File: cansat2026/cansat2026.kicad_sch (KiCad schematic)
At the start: 29 parts, among them J102 MCU_UART_Conn, J103 MCU_CAM_UART_Conn, J104 920MHz_Conn, J105 I2C_Conn, J106 I2C_Conn, J117 CAM_Conn, J121 MCU_Power, J122 MCU_Power, J124 Motor_Power, J126 Micro_SD_Card_Det_Hirose_DM3AT, U101 ESP32-S3-WROOM-1U-N4R8, U102 ESP32-S3-WROOM-1U-N4R8

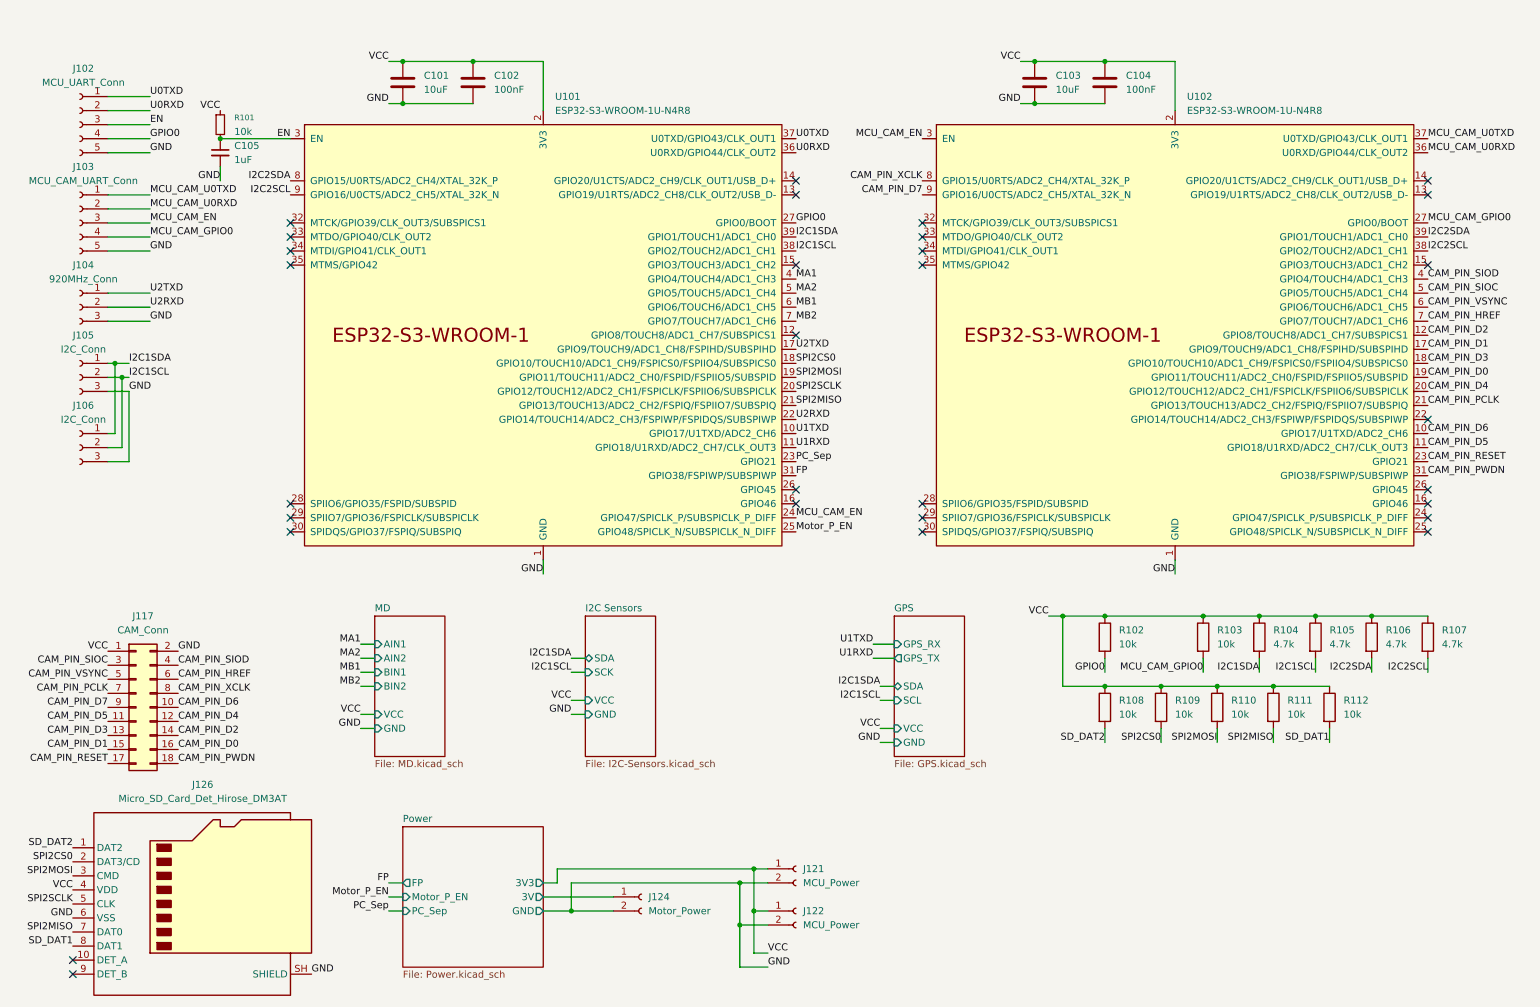
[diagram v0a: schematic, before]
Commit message: Update: MCUシートを作成
MCU部分を分けた
あとでFPGAつけるかもしれないしね
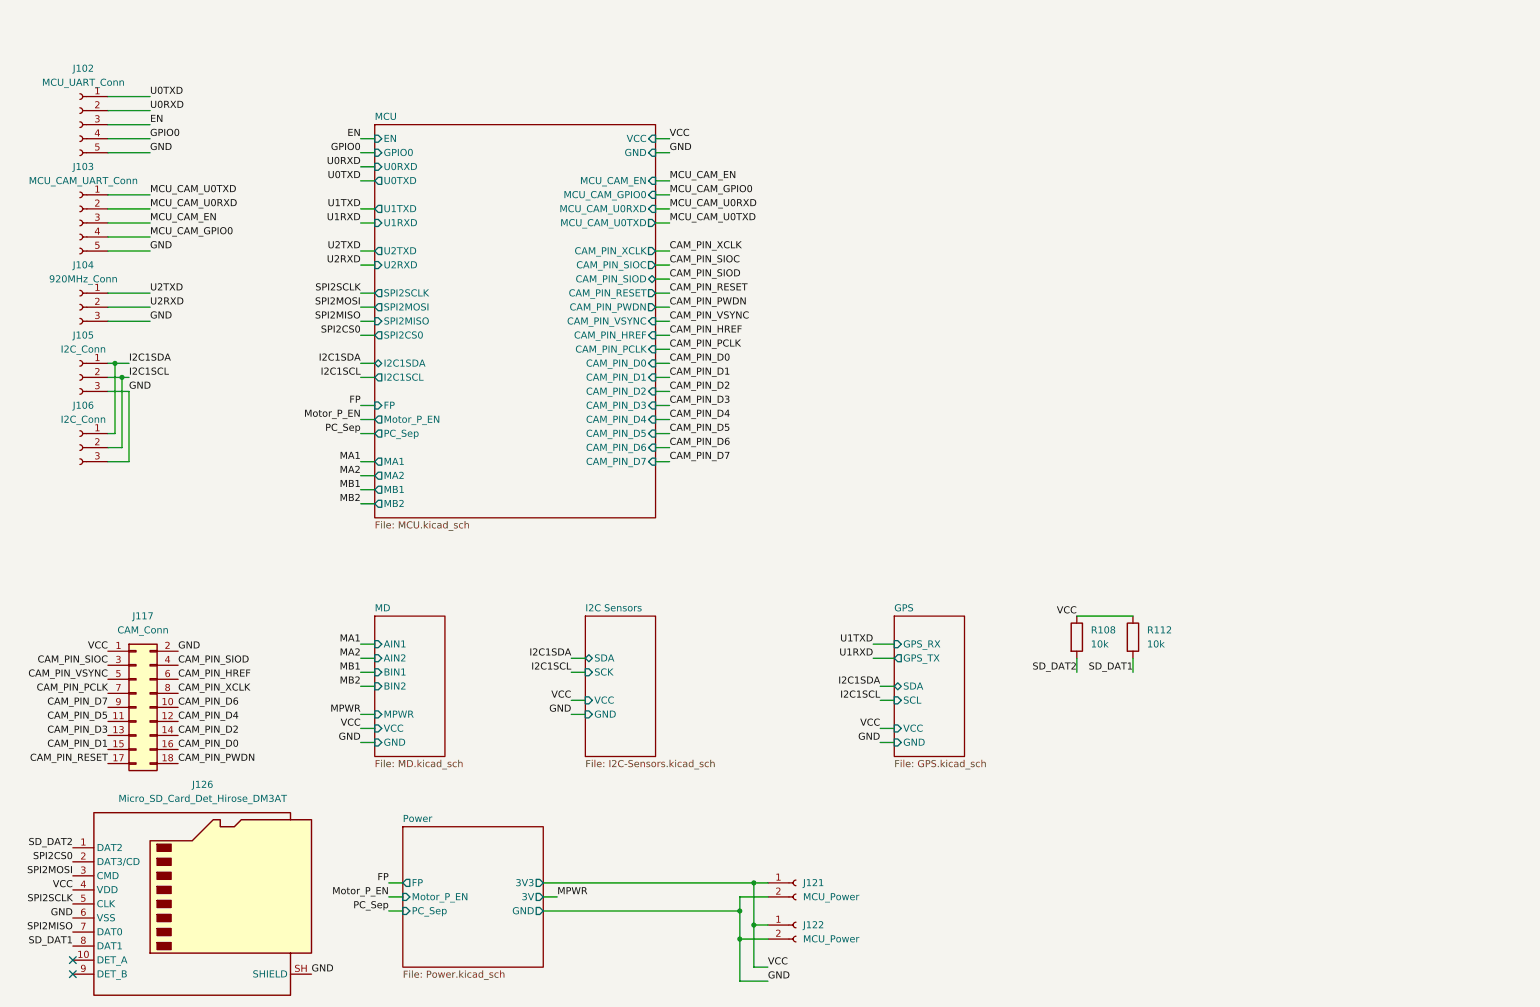
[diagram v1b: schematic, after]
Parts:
- removed C101, C103: 10uF, Capacitor_SMD:C_0402_1005Metric, symbol Device:C
- removed C102, C104: 100nF, Capacitor_SMD:C_0402_1005Metric, symbol Device:C
- removed C105: 1uF, Capacitor_SMD:C_0402_1005Metric, symbol Device:C_Small
- removed J124: Motor_Power, Connector_JST:JST_XH_B2B-XH-A_1x02_P2.50mm_Vertical, symbol Connector:Conn_01x02_Socket
- removed R101: 10k, Resistor_SMD:R_0402_1005Metric, symbol Device:R_Small
- removed R102, R103, R109, R110, R111: 10k, Resistor_SMD:R_0402_1005Metric, symbol Device:R
- removed R104, R105, R106, R107: 4.7k, Resistor_SMD:R_0402_1005Metric, symbol Device:R
- removed U101, U102: ESP32-S3-WROOM-1U-N4R8, PCM_Espressif:ESP32-S3-WROOM-1U, symbol PCM_Espressif:ESP32-S3-WROOM-1
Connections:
- no-connect marks 30 -> 2
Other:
- added sheet MCU (MCU.kicad_sch)
- sheet MD ports: added MPWR; removed none
- moved on the sheet: J121, J122

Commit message: Update: ラベルをワイヤーにした
ラベルが衝突してERCが出たから
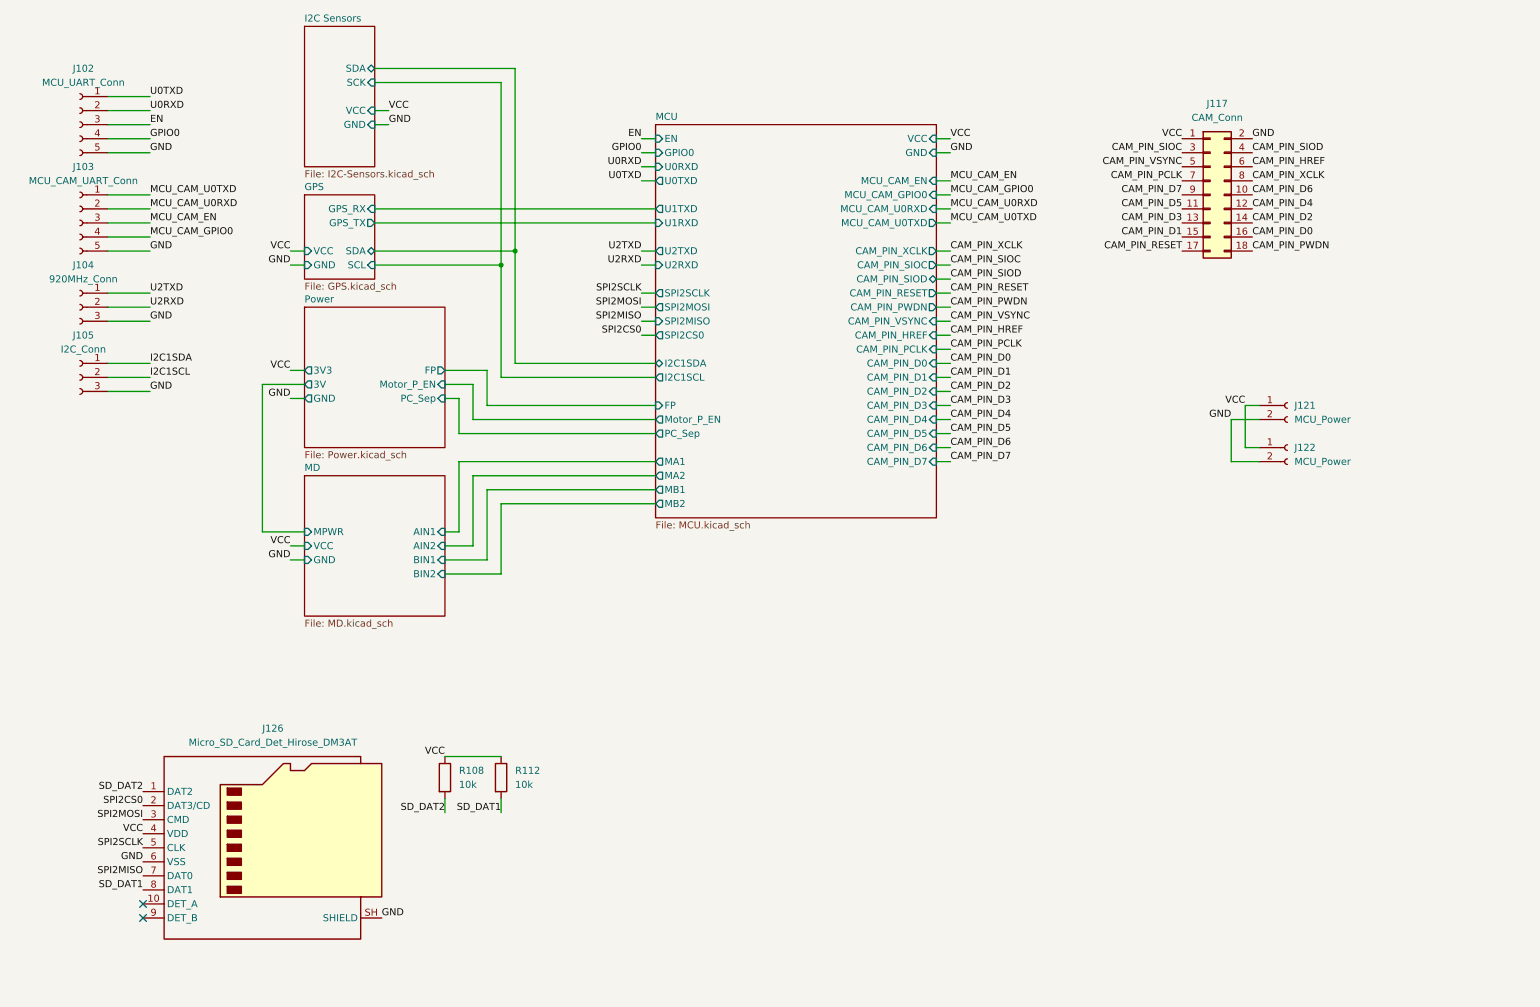
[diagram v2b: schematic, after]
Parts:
- removed J106: I2C_Conn, Connector_JST:JST_XH_B3B-XH-A_1x03_P2.50mm_Vertical, symbol Connector:Conn_01x03_Socket
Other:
- moved on the sheet: J117, J121, J122, J126, R108, R112

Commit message: Update: いろいろした
無線変えた
カメラのコネクタ変えた
i2cセンサ変えた
電源変えた:1.2V,3.8V,3.3V
IOエキスパンダ追加
FPGA追加
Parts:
- removed J104: 920MHz_Conn, Connector_JST:JST_XH_B3B-XH-A_1x03_P2.50mm_Vertical, symbol Connector:Conn_01x03_Socket
- removed J117: CAM_Conn, Connector_PinHeader_2.54mm:PinHeader_2x10_P2.54mm_Vertical, symbol Connector_Generic:Conn_02x09_Odd_Even
- added C101: 100nF, Capacitor_SMD:C_0402_1005Metric, symbol Device:C_Small
- added C102: 100nF, Capacitor_SMD:C_0402_1005Metric, symbol Device:C
- added J102: CAM_Conn, Project:SHOUHAN_XJH2.0_0.43-24P_1x24-1MP_P0.50mm_Horizontal, symbol Connector_Generic_MountingPin:Conn_02x12_Odd_Even_MountingPin
- added J108: Conn_Coaxial, Connector_Coaxial:SMA_Samtec_SMA-J-P-H-ST-EM1_EdgeMount, symbol Connector:Conn_Coaxial
- added U101: E220-900T22S(JP), Project:E220-900T22S(JP), symbol Project:E220-900T22S(JP)
- renumbered J102 to J101, J105 to J104, J121 to J105, J122 to J106, J126 to J107, R108 to R101, R112 to R102
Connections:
- net CAM_PIN_D0: now also J102.23 (Pin_23)
- net CAM_PIN_D1: now also J102.22 (Pin_22)
- net CAM_PIN_D2: now also J102.21 (Pin_21)
- net CAM_PIN_D3: now also J102.20 (Pin_20)
- net CAM_PIN_D4: now also J102.19 (Pin_19)
- net CAM_PIN_D5: now also J102.18 (Pin_18)
- net CAM_PIN_D6: now also J102.17 (Pin_17)
- net CAM_PIN_D7: now also J102.16 (Pin_16)
- net CAM_PIN_HREF: now also J102.12 (Pin_12)
- net CAM_PIN_PCLK: now also J102.14 (Pin_14)
- net CAM_PIN_PWDN: now also J102.5 (Pin_5)
- net CAM_PIN_RESET: now also J102.6 (Pin_6)
- net CAM_PIN_SIOC: now also J102.3 (Pin_3)
- net CAM_PIN_SIOD: now also J102.4 (Pin_4)
- net CAM_PIN_VSYNC: now also J102.11 (Pin_11)
- net CAM_PIN_XCLK: now also J102.8 (Pin_8)
- net GND: now also C101.2, C102.2, J102.13 (Pin_13), J102.15 (Pin_15), J102.24 (Pin_24), J102.7 (Pin_7), J102.9 (Pin_9), J102.MP (MountPin), J108.2 (Ext), U101.1 (GND), U101.11 (GND), U101.19 (GND), U101.2 (GND), U101.20 (GND), U101.22 (GND), U101.3 (GND), U101.4 (GND)
- net U2RXD: now also U101.8 (TXD)
- net U2TXD: now also U101.7 (RXD)
- net VCC: now also J102.1 (Pin_1), J102.2 (Pin_2)
- new net: J108.1 (In), U101.21 (ANT)
- new net: U101.16 (NC), U101.17 (NC), U101.18 (NC)
- new net 3.8V: C101.1, U101.10 (VCC)
- new net COM_AUX: C102.1, U101.9 (AUX)
- new net COM_M0: U101.5 (M0)
- new net COM_M1: U101.6 (M1)
- no-connect marks 2 -> 7
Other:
- sheet MCU ports: added 1.2V, COM_AUX, COM_M0, COM_M1, COM_P_EN; removed none
- sheet Power ports: added 1.2V, 3.8V, COM_P_EN; removed none
- moved on the sheet: J104

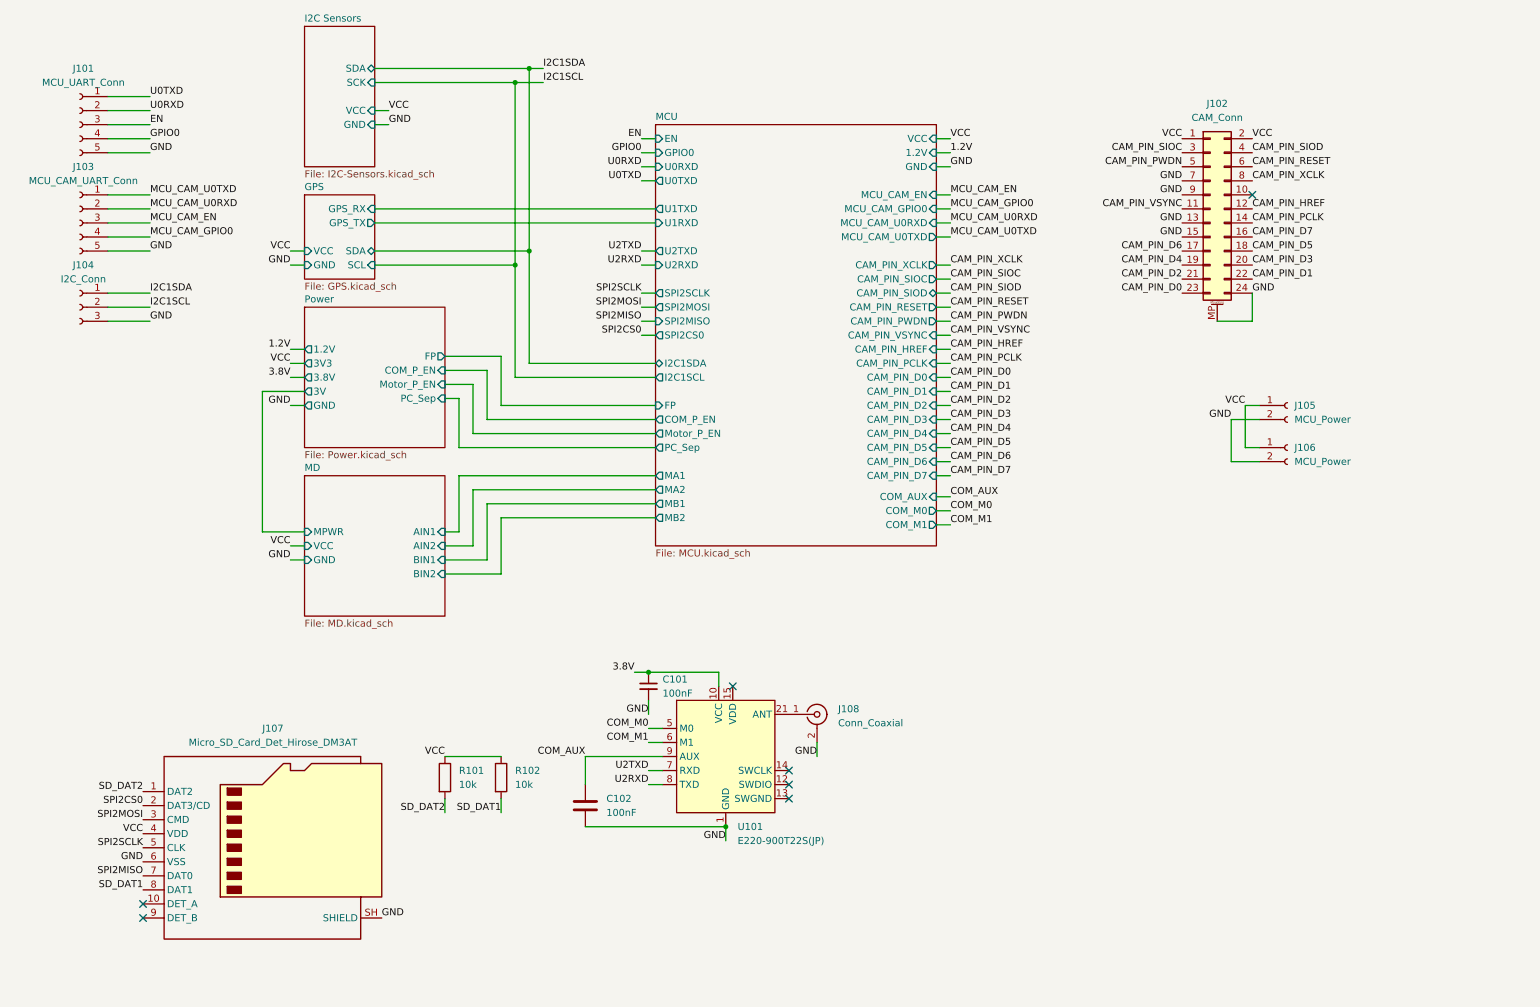
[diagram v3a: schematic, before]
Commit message: Update: MDと電源とか
MD変えた
モーター電源と主電源
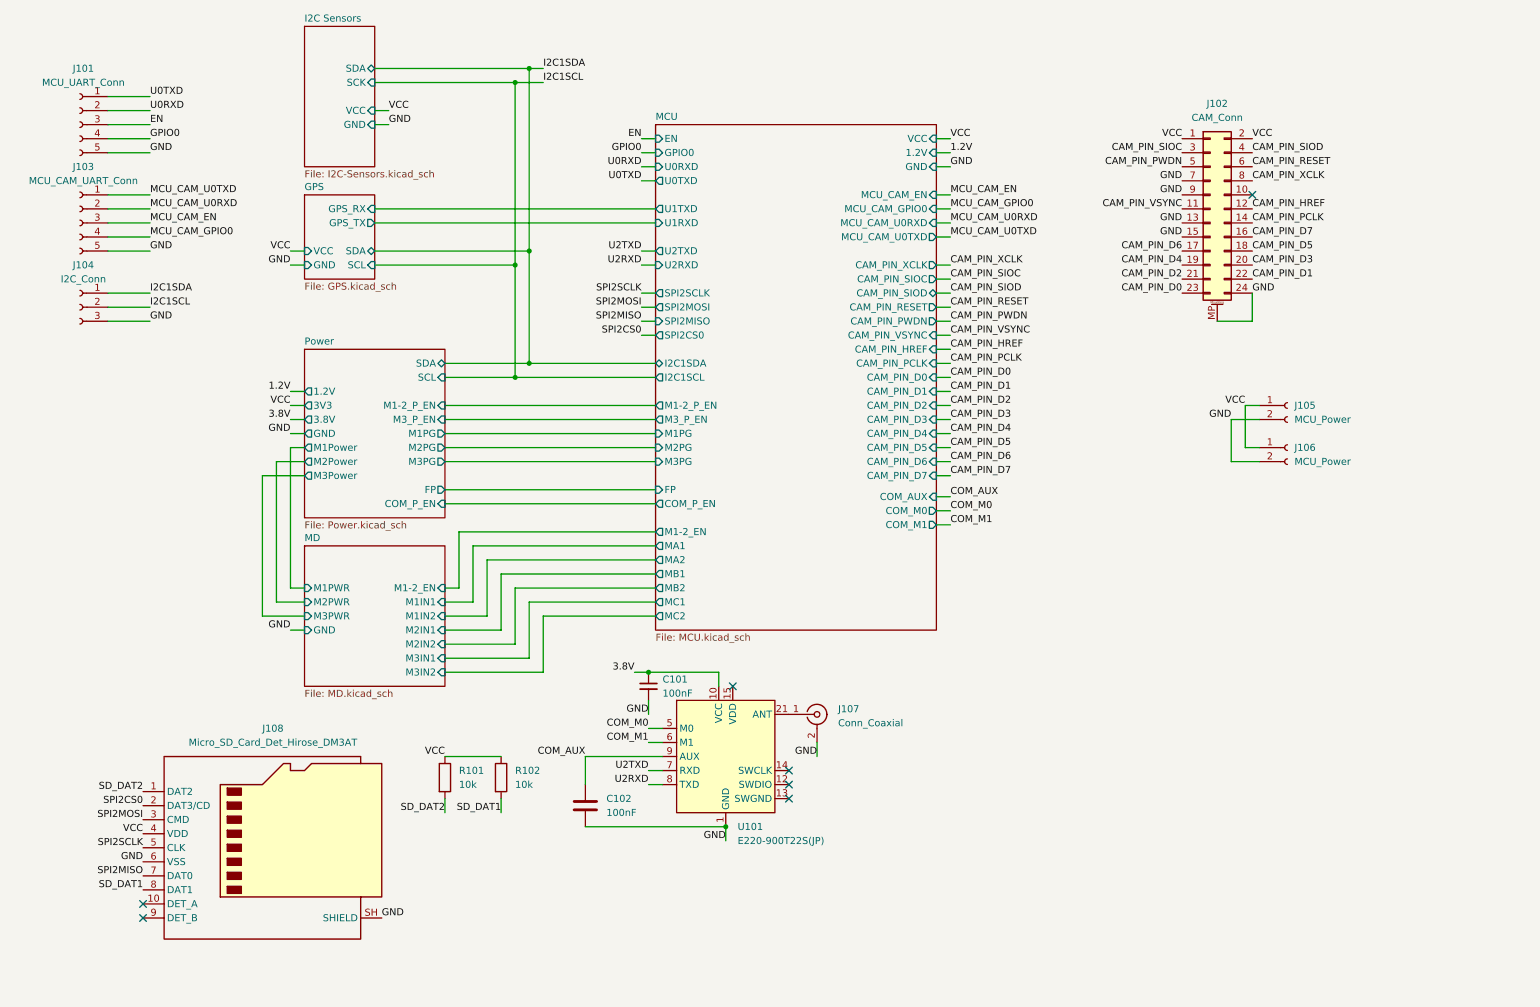
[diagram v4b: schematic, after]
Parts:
- renumbered J108 to J107, J107 to J108
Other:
- sheet MCU ports: added M1-2_EN, M1-2_P_EN, M1PG, M2PG, M3PG, M3_P_EN, MC1, MC2; removed Motor_P_EN, PC_Sep
- sheet MD ports: added M1-2_EN, M1IN1, M1IN2, M1PWR, M2IN1, M2IN2, M2PWR, M3IN1, M3IN2, M3PWR; removed AIN1, AIN2, BIN1, BIN2, MPWR, VCC
- sheet Power ports: added M1-2_P_EN, M1PG, M1Power, M2PG, M2Power, M3PG, M3Power, M3_P_EN, SCL, SDA; removed 3V, Motor_P_EN, PC_Sep

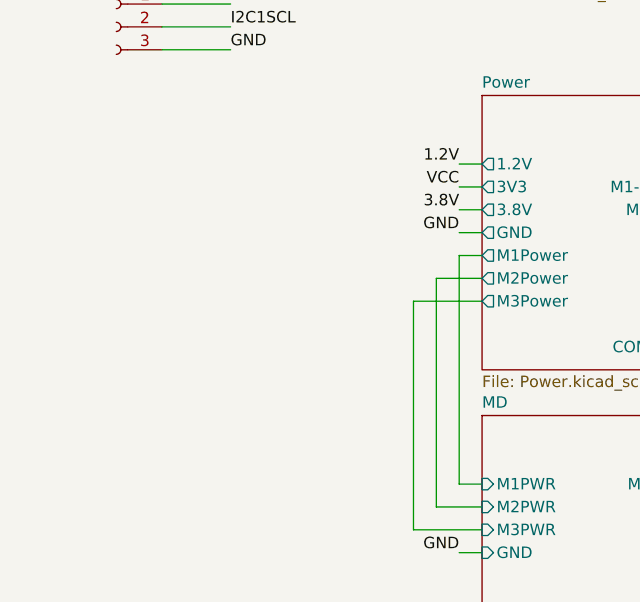
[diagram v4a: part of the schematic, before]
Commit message: Update: いろいろした
GPS変えた
USB追加した
気圧センサ変えた
FPGA変えた
MDにキャパシタ追加した
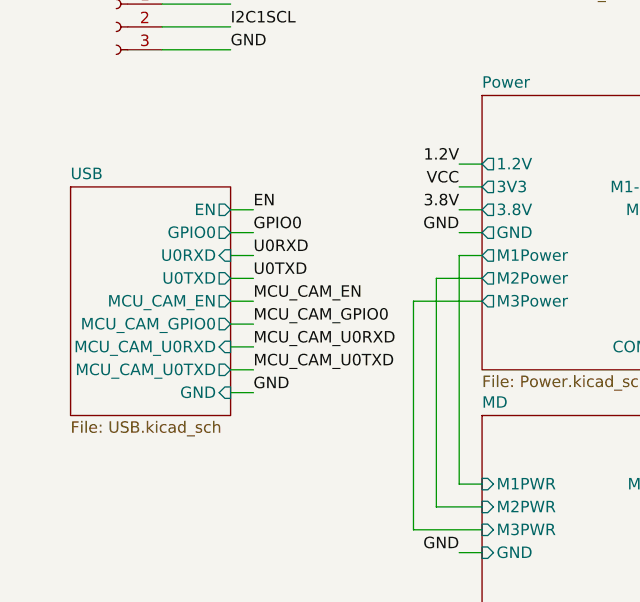
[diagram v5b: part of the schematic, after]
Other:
- added sheet USB (USB.kicad_sch)

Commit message: Update: 完成した
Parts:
- removed J107: Conn_Coaxial, Connector_Coaxial:SMA_Samtec_SMA-J-P-H-ST-EM1_EdgeMount, symbol Connector:Conn_Coaxial
- J101, J103: 秋月 Part (none) -> 105779
- J102: LCSC Part (none) -> C5373439
- J104: 秋月 Part (none) -> 112248
- J105, J106: 秋月 Part (none) -> 112247
- J107: renamed from J108; 秋月 Part (none) -> 102395
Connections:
- no-connect marks 7 -> 8
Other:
- sheet MCU ports: added 1.8V; removed none
- sheet Power ports: added 1.8V; removed none
